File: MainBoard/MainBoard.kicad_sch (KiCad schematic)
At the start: 56 parts, among them J2 Non-Inverting Input, J3 Inverting Input, J4 Output, J5 InvertedOutput, J6 Inverting Input, J7 Non-Inverting Input, J8 Output, J9 InvertedOutput, Q16 BC557, Q32 BC557

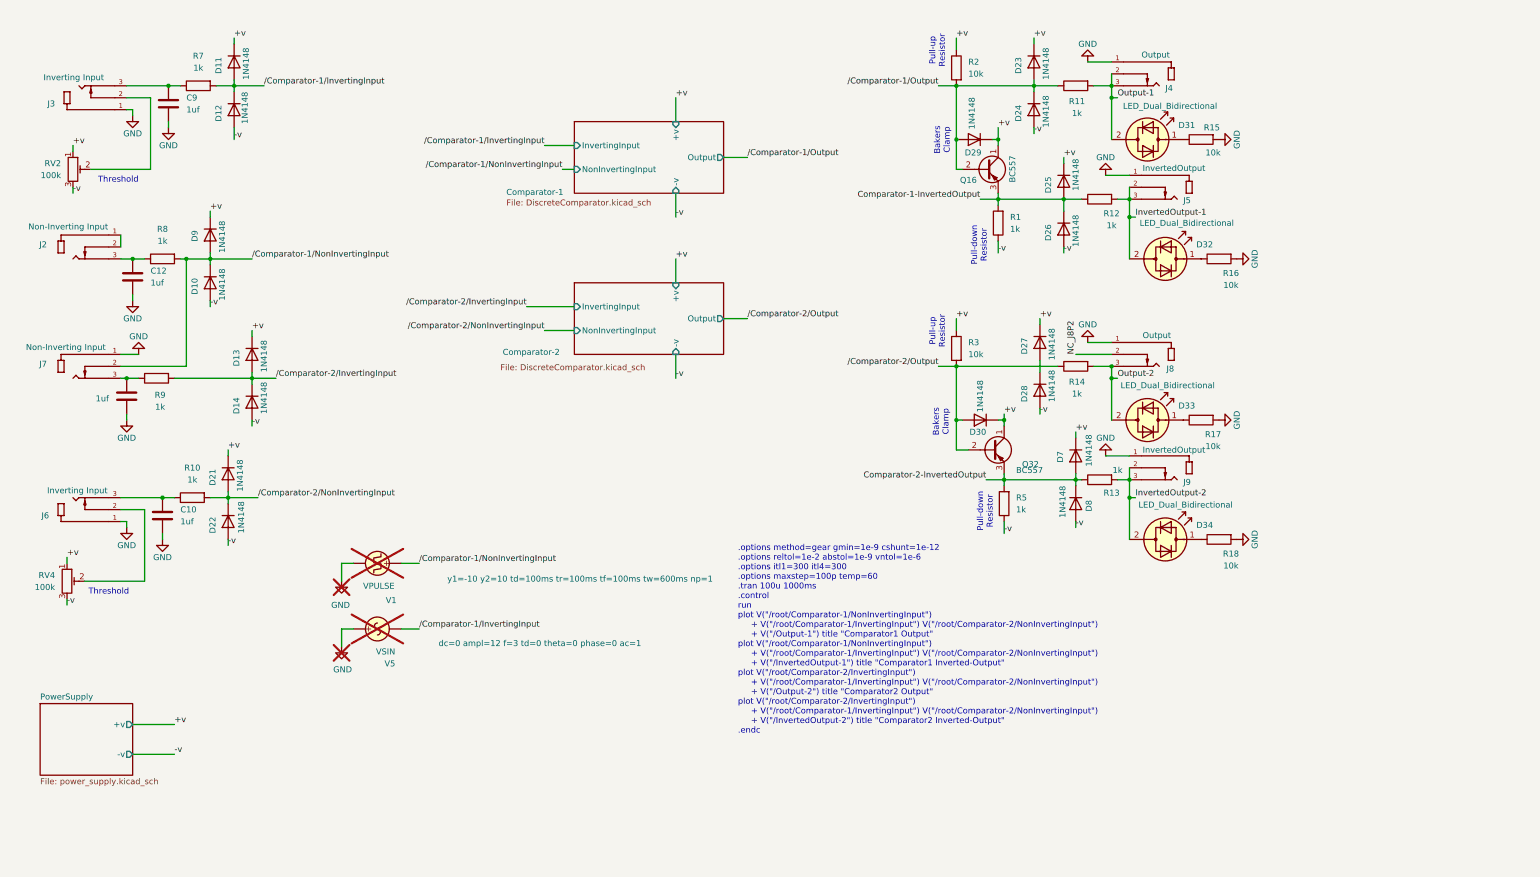
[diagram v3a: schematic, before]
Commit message: functional -- but very slow slew rates
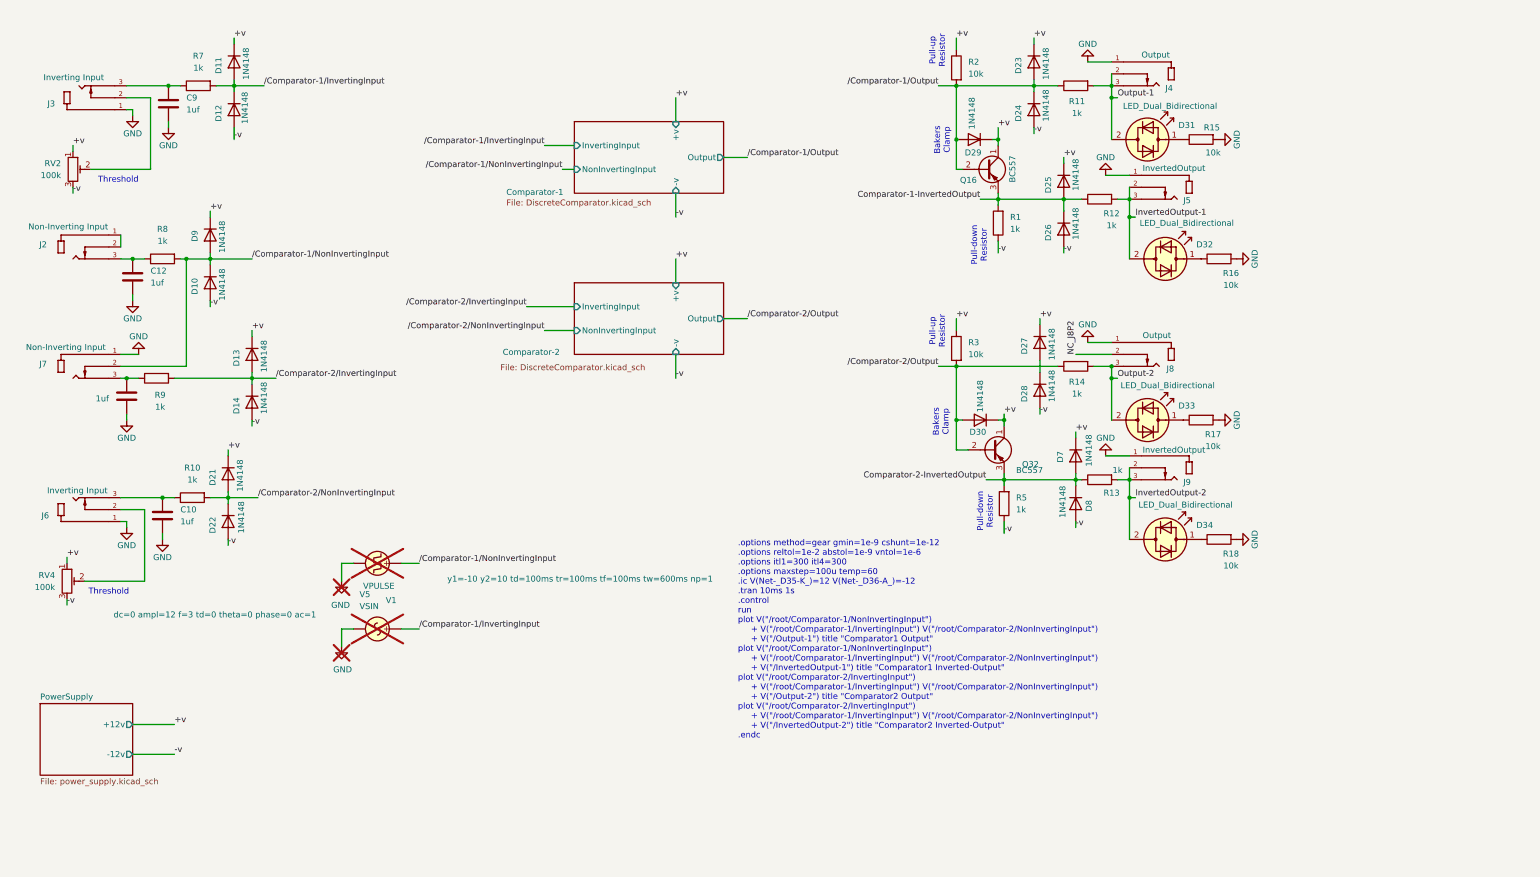
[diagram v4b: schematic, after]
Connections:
- net GND: now also V5.2; no longer V5.1
- net /Comparator-1/InvertingInput: now also V5.1; no longer V5.2
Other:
- sheet PowerSupply ports: added +12v, -12v; removed +v, -v
- note added: ".options method=gear gmin=1e-9 cshunt=1e-12 .options reltol=1e-2 abstol=1e-9 vntol=1e-6 .options itl1=300 itl4=300 .options maxstep=100u temp=60 .ic V(Net-_D35-K_)=12 V(Net-_D36-A_)=-12 .tran 10ms 1s .control run plot V("/root/Comparator-1/NonInvertingInput") + V("/root/Comparator-1/InvertingInput") V("/root/Comparator-2/NonInvertingInput") + V("/Output-1") title "Comparator1 Output" plot V("/roo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"
- note removed: ".options method=gear gmin=1e-9 cshunt=1e-12 .options reltol=1e-2 abstol=1e-9 vntol=1e-6 .options itl1=300 itl4=300 .options maxstep=100p temp=60 .tran 100u 1000ms .control run plot V("/root/Comparator-1/NonInvertingInput") + V("/root/Comparator-1/InvertingInput") V("/root/Comparator-2/NonInvertingInput") + V("/Output-1") title "Comparator1 Output" plot V("/root/Comparator-1/NonInvertingInput") + 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"
- moved on the sheet: V5
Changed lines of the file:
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@@
 		)
 	)
-	(text ".options method=gear gmin=1e-9 cshunt=1e-12 \n.options reltol=1e-2 abstol=1e-9 vntol=1e-6 \n.options itl1=300 itl4=300 \n.options maxstep=100p temp=60\n.tran 100u 1000ms\n.control\nrun\nplot V(\"/root/Comparator-1/NonInvertingInput\") \n     + V(\"/root/Comparator-1/InvertingInput\") V(\"/root/Comparator-2/NonInvertingInput\") \n     + V(\"/Output-1\") title \"Comparator1 Output\" \nplot V(\"/root/Comparator-1/NonInvertingInput\")\n     + V(\"/root/Comparator-1/InvertingInput\") V(\"/root/Comparator-2/NonInvertingInput\") \n     + V(\"/InvertedOutput-1\") title \"Comparator1 Inverted-Output\"\nplot V(\"/root/Comparator-2/InvertingInput\") \n     + V(\"/root/Comparator-1/InvertingInput\") V(\"/root/Comparator-2/NonInvertingInput\")   \n     + V(\"/Output-2\") title \"Comparator2 Output\" \nplot V(\"/root/Comparator-2/InvertingInput\")\n     + V(\"/root/Comparator-1/InvertingInput\") V(\"/root/Comparator-2/NonInvertingInput\") \n     + V(\"/InvertedOutput-2\") title \"Comparator2 Inverted-Output\"\n.endc"
+	(text ".options method=gear gmin=1e-9 cshunt=1e-12 \n.options reltol=1e-2 abstol=1e-9 vntol=1e-6 \n.options itl1=300 itl4=300 \n.options maxstep=100u temp=60\n.ic V(Net-_D35-K_)=12 V(Net-_D36-A_)=-12\n.tran 10ms 1s\n.control\nrun\nplot V(\"/root/Comparator-1/NonInvertingInput\") \n     + V(\"/root/Comparator-1/InvertingInput\") V(\"/root/Comparator-2/NonInvertingInput\") \n     + V(\"/Output-1\") title \"Comparator1 Output\" \nplot V(\"/root/Comparator-1/NonInvertingInput\")\n     + V(\"/root/Comparator-1/InvertingInput\") V(\"/root/Comparator-2/NonInvertingInput\") \n     + V(\"/InvertedOutput-1\") title \"Comparator1 Inverted-Output\"\nplot V(\"/root/Comparator-2/InvertingInput\") \n     + V(\"/root/Comparator-1/InvertingInput\") V(\"/root/Comparator-2/NonInvertingInput\")   \n     + V(\"/Output-2\") title \"Comparator2 Output\" \nplot V(\"/root/Comparator-2/InvertingInput\")\n     + V(\"/root/Comparator-1/InvertingInput\") V(\"/root/Comparator-2/NonInvertingInput\") \n     + V(\"/InvertedOutput-2\") title \"Comparator2 Inverted-Output\"\n.endc"
 		(exclude_from_sim no)
 		(at 170.688 147.066 0)
@@
 		)
 		(property "Value" "1N4148"
-			(at 242.57 56.642 0)
+			(at 242.57 55.118 0)
 			(effects
 				(font
@@
 	(symbol
 		(lib_id "Simulation_SPICE:VSIN")
-		(at 93.98 144.78 90)
+		(at 93.98 144.78 270)
 		(mirror x)
 		(unit 1)
@@
 		(dnp yes)
 		(property "Reference" "V5"
-			(at 97.79 152.146 90)
+			(at 90.17 137.414 90)
 			(effects
 				(font
@@
 		)
 		(property "Value" "VSIN"
-			(at 97.79 149.606 90)
+			(at 90.17 139.954 90)
 			(effects
 				(font
@@
 		)
 		(property "Sim.Params" "dc=0 ampl=12 f=3 td=0 theta=0 phase=0 ac=1"
-			(at 150.114 147.828 90)
+			(at 37.846 141.732 90)
 			(effects
 				(font
@@
 		)
 		(property "Value" "1N4148"
-			(at 236.22 31.242 0)
+			(at 236.22 29.972 0)
 			(effects
 				(font
@@
 			)
 		)
-		(pin "+v" output
+		(pin "+12v" output
 			(at 41.91 165.1 0)
 			(effects
@@
 			)
 		)
-		(pin "-v" output
+		(pin "-12v" output
 			(at 41.91 171.45 0)
 			(effects

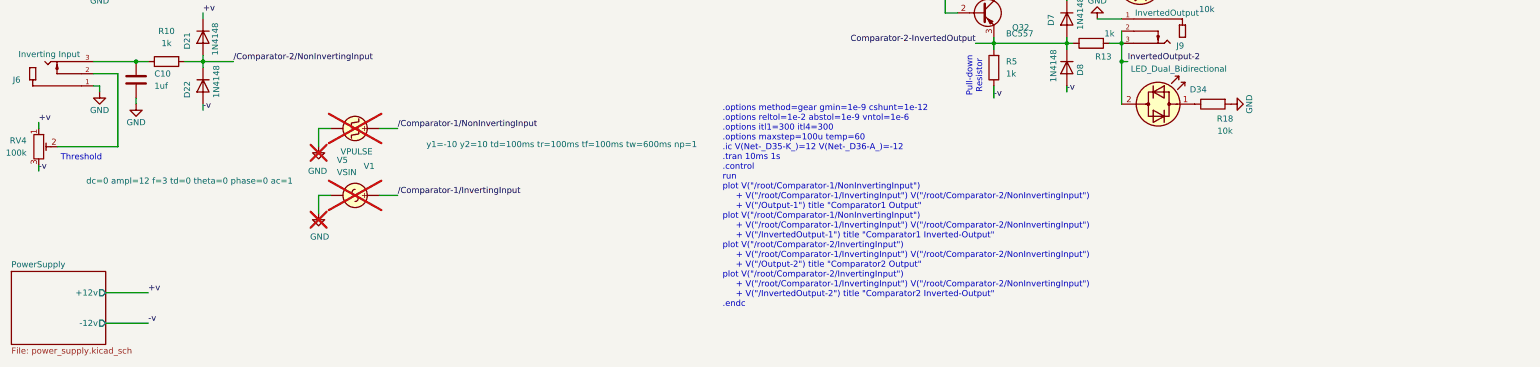
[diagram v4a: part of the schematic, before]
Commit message: added power supply
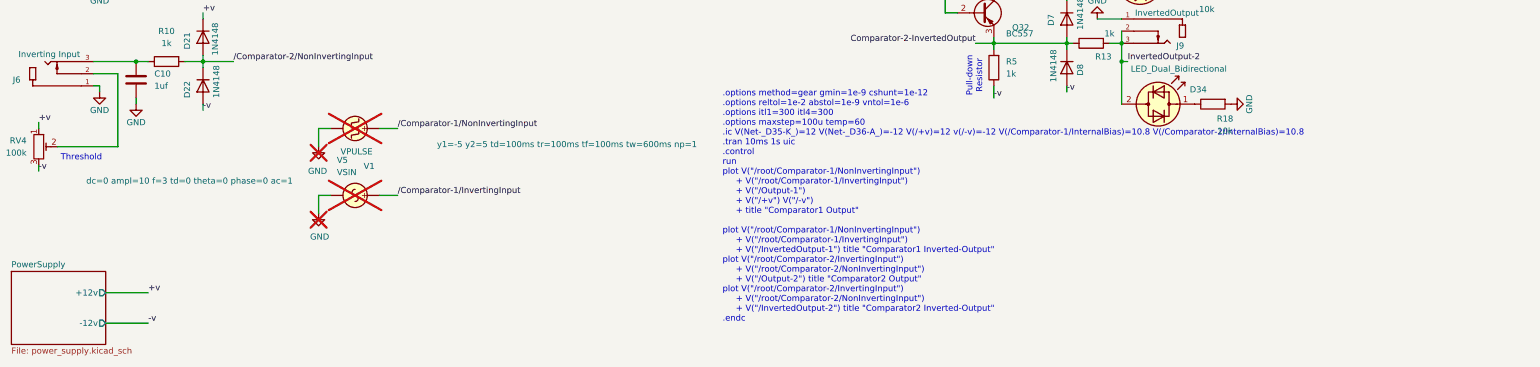
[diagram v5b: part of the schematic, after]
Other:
- note added: ".options method=gear gmin=1e-9 cshunt=1e-12 .options reltol=1e-2 abstol=1e-9 vntol=1e-6 .options itl1=300 itl4=300 .options maxstep=100u temp=60 .ic V(Net-_D35-K_)=12 V(Net-_D36-A_)=-12 V(/+v)=12 v(/-v)=-12 V(/Comparator-1/InternalBias)=10.8 V(/Comparator-2/InternalBias)=10.8 .tran 10ms 1s uic .control run plot V("/root/Comparator-1/NonInvertingInput") + V("/root/Comparator-1/InvertingInput") + V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"
- note removed: ".options method=gear gmin=1e-9 cshunt=1e-12 .options reltol=1e-2 abstol=1e-9 vntol=1e-6 .options itl1=300 itl4=300 .options maxstep=100u temp=60 .ic V(Net-_D35-K_)=12 V(Net-_D36-A_)=-12 .tran 10ms 1s .control run plot V("/root/Comparator-1/NonInvertingInput") + V("/root/Comparator-1/InvertingInput") V("/root/Comparator-2/NonInvertingInput") + V("/Output-1") title "Comparator1 Output" plot V("/roo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"
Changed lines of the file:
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@@
 		)
 	)
-	(text ".options method=gear gmin=1e-9 cshunt=1e-12 \n.options reltol=1e-2 abstol=1e-9 vntol=1e-6 \n.options itl1=300 itl4=300 \n.options maxstep=100u temp=60\n.ic V(Net-_D35-K_)=12 V(Net-_D36-A_)=-12\n.tran 10ms 1s\n.control\nrun\nplot V(\"/root/Comparator-1/NonInvertingInput\") \n     + V(\"/root/Comparator-1/InvertingInput\") V(\"/root/Comparator-2/NonInvertingInput\") \n     + V(\"/Output-1\") title \"Comparator1 Output\" \nplot V(\"/root/Comparator-1/NonInvertingInput\")\n     + V(\"/root/Comparator-1/InvertingInput\") V(\"/root/Comparator-2/NonInvertingInput\") \n     + V(\"/InvertedOutput-1\") title \"Comparator1 Inverted-Output\"\nplot V(\"/root/Comparator-2/InvertingInput\") \n     + V(\"/root/Comparator-1/InvertingInput\") V(\"/root/Comparator-2/NonInvertingInput\")   \n     + V(\"/Output-2\") title \"Comparator2 Output\" \nplot V(\"/root/Comparator-2/InvertingInput\")\n     + V(\"/root/Comparator-1/InvertingInput\") V(\"/root/Comparator-2/NonInvertingInput\") \n     + V(\"/InvertedOutput-2\") title \"Comparator2 Inverted-Output\"\n.endc"
+	(text ".options method=gear gmin=1e-9 cshunt=1e-12 \n.options reltol=1e-2 abstol=1e-9 vntol=1e-6 \n.options itl1=300 itl4=300 \n.options maxstep=100u temp=60\n.ic V(Net-_D35-K_)=12 V(Net-_D36-A_)=-12 V(/+v)=12 v(/-v)=-12 V(/Comparator-1/InternalBias)=10.8 V(/Comparator-2/InternalBias)=10.8\n.tran 10ms 1s uic\n.control\nrun\nplot V(\"/root/Comparator-1/NonInvertingInput\") \n     + V(\"/root/Comparator-1/InvertingInput\") \n     + V(\"/Output-1\")\n     + V(\"/+v\") V(\"/-v\")\n     + title \"Comparator1 Output\" \n    \nplot V(\"/root/Comparator-1/NonInvertingInput\")\n     + V(\"/root/Comparator-1/InvertingInput\")\n     + V(\"/InvertedOutput-1\") title \"Comparator1 Inverted-Output\"\nplot V(\"/root/Comparator-2/InvertingInput\") \n     + V(\"/root/Comparator-2/NonInvertingInput\")   \n     + V(\"/Output-2\") title \"Comparator2 Output\" \nplot V(\"/root/Comparator-2/InvertingInput\")\n     + V(\"/root/Comparator-2/NonInvertingInput\") \n     + V(\"/InvertedOutput-2\") title \"Comparator2 Inverted-Output\"\n.endc"
 		(exclude_from_sim no)
 		(at 170.688 147.066 0)
@@
 			)
 		)
-		(property "Sim.Params" "y1=-10 y2=10 td=100ms tr=100ms tf=100ms tw=600ms np=1"
+		(property "Sim.Params" "y1=-5 y2=5 td=100ms tr=100ms tf=100ms tw=600ms np=1"
 			(at 165.354 134.112 90)
 			(effects
@@
 			)
 		)
-		(property "Sim.Params" "dc=0 ampl=12 f=3 td=0 theta=0 phase=0 ac=1"
+		(property "Sim.Params" "dc=0 ampl=10 f=3 td=0 theta=0 phase=0 ac=1"
 			(at 37.846 141.732 90)
 			(effects
